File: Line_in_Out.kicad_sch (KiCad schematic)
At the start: 10 parts, among them J4 Out Left, J5 Out Right

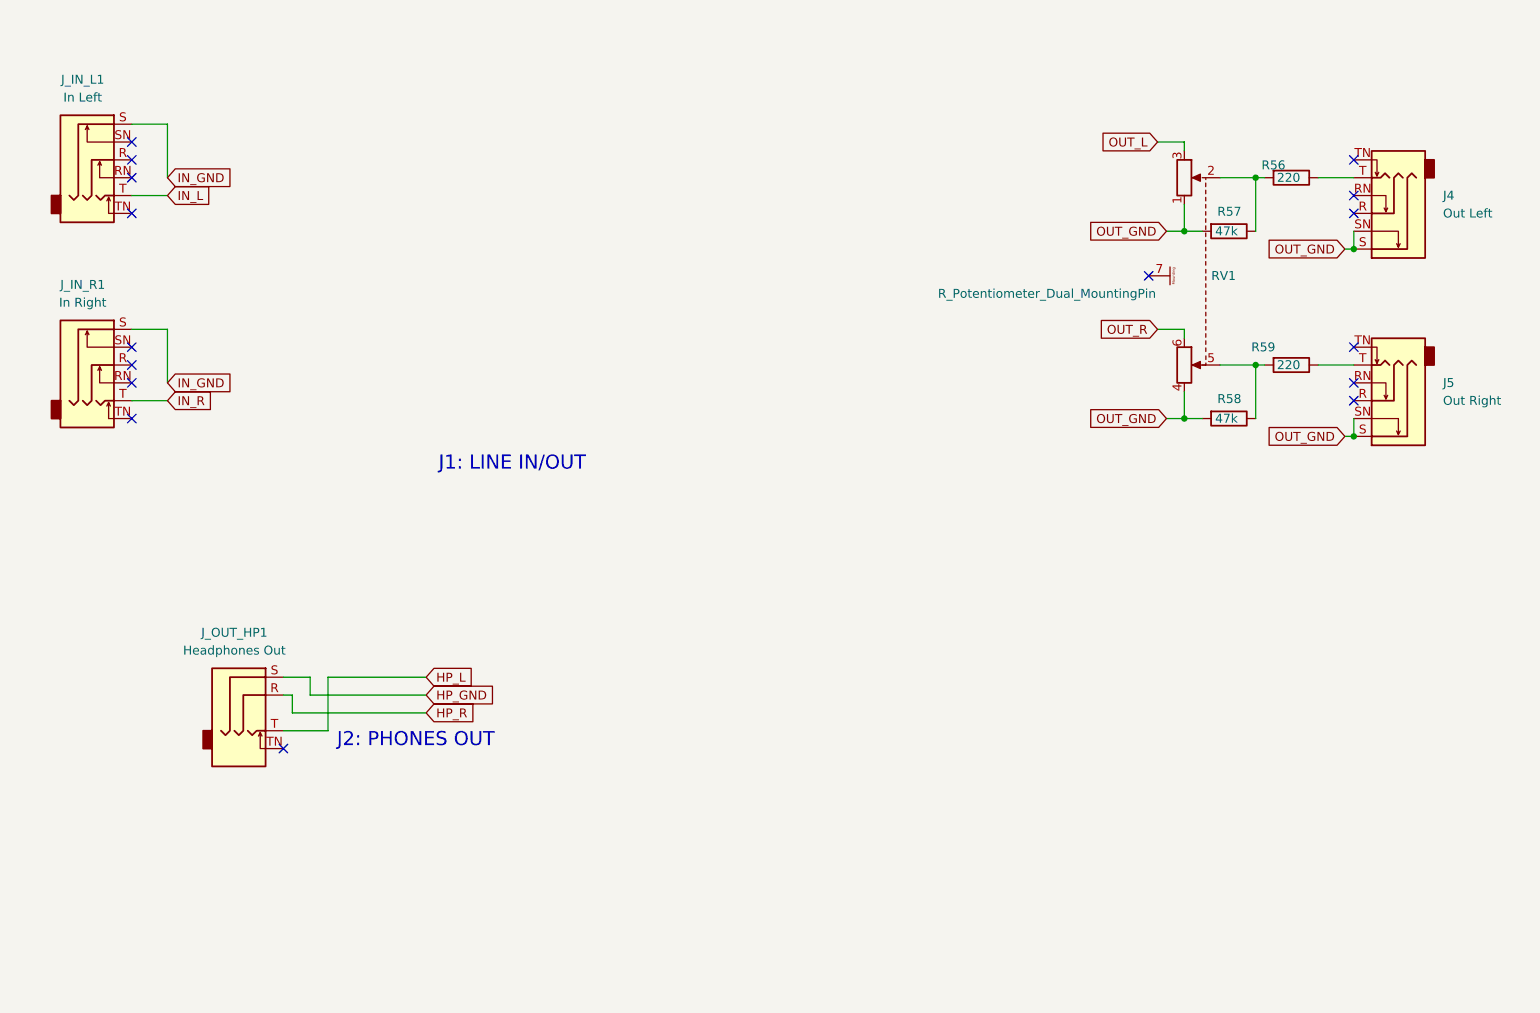
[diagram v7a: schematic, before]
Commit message: Added jack symbols and footprints also footprints for ics and caps
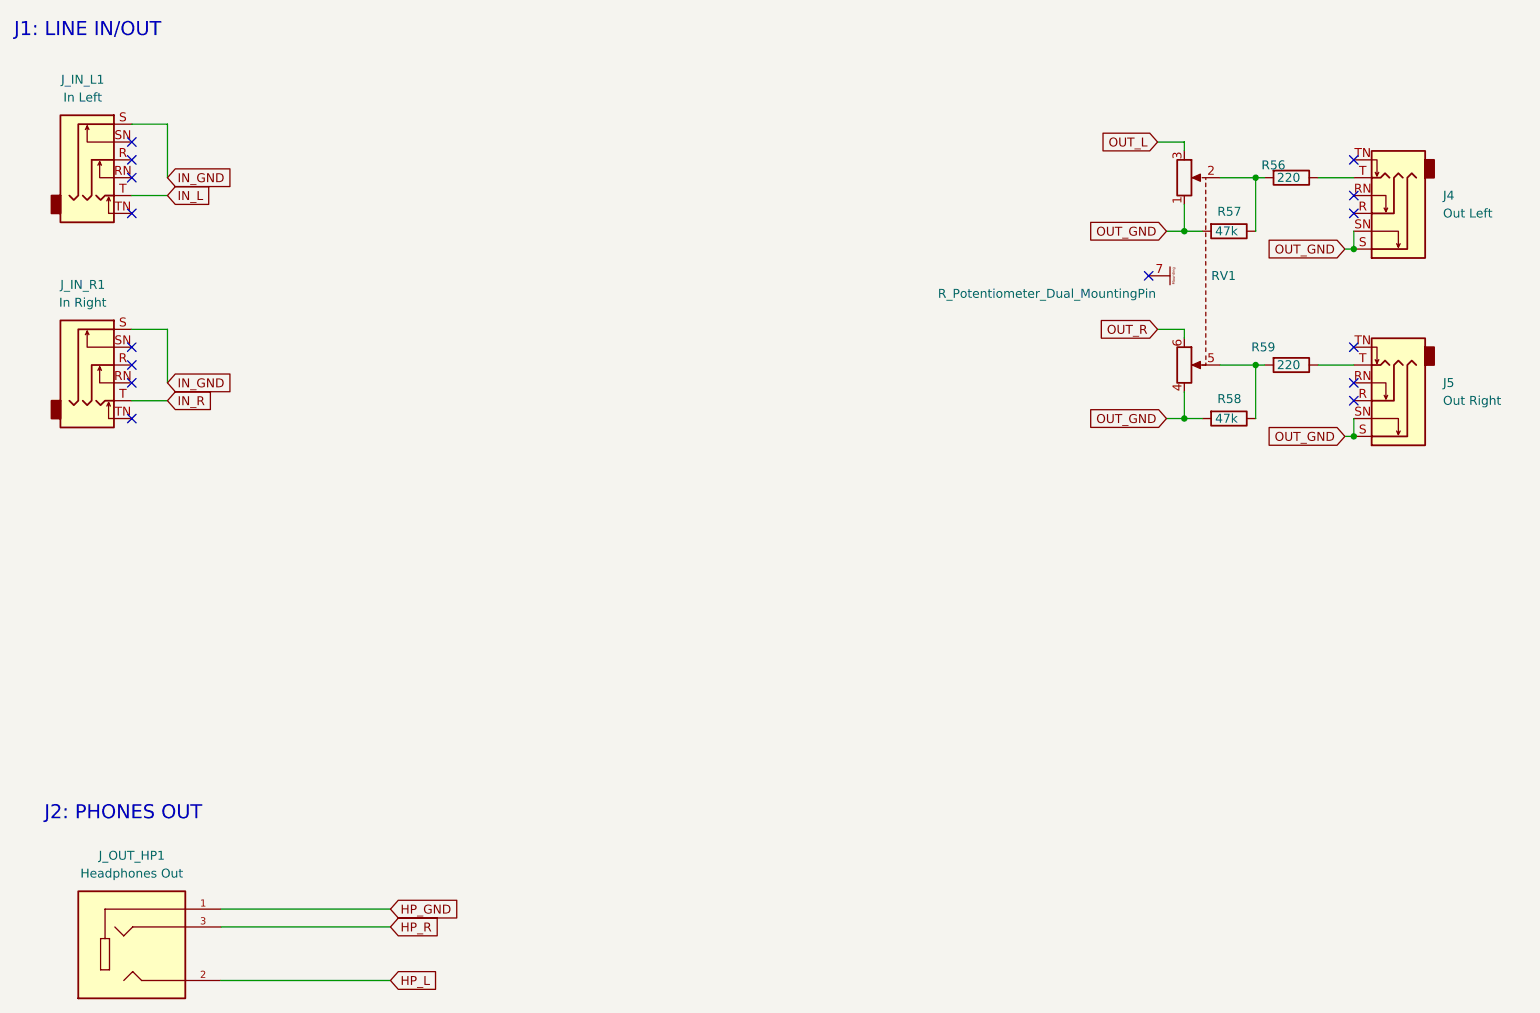
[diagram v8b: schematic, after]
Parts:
- J_OUT_HP1: footprint Connector_Audio:Jack_3.5mm_CUI_SJ1-3513N_Horizontal -> diggi_footprints:CUI_SJ1-3523N; symbol ksoloti_shield_symbols:AudioJack3_3.5mm_Stereo_SwitchT_WQP729JH-Blue_from_Thonk -> SJ1-3523N:SJ1-3523N; Availability (none) -> In Stock; Check_prices (none) -> https://www.snapeda.com/parts/SJ1-3523N/Same+Sky/view-part/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; Description_1 (none) -> 3.5 mm, Stereo, Right Angle, Through Hole, 3 Conductors, 0 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; MANUFACTURER (none) -> CUI Devices; MAXIMUM_PACKAGE_HEIGHT (none) -> 6.25 mm; MF (none) -> Same Sky; MP (none) -> SJ1-3523N; PARTREV (none) -> 1.05; Package (none) -> None; Price (none) -> None; Purchase-URL (none) -> https://www.snapeda.com/api/url_track_click_mouser/?unipart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; STANDARD (none) -> Manufacturer Recommendations; SnapEDA_Link (none) -> https://www.snapeda.com/parts/SJ1-3523N/Same+Sky/view-part/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
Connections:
- net HP_GND: now also J_OUT_HP1.1; no longer J_OUT_HP1.S
- net HP_L: now also J_OUT_HP1.2; no longer J_OUT_HP1.T
- net HP_R: now also J_OUT_HP1.3; no longer J_OUT_HP1.R
- no-connect marks 16 -> 15
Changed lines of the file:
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@@
 	(text "J2: PHONES OUT"
 		(exclude_from_sim no)
-		(at 87.63 128.27 0)
+		(at 45.974 138.684 0)
 		(effects
 			(font
@@
 	(text "J1: LINE IN/OUT"
 		(exclude_from_sim no)
-		(at 102.108 88.9 0)
+		(at 41.656 27.178 0)
 		(effects
 			(font
@@
 	)
 	(no_connect
-		(at 80.01 128.27)
-	)
-	(no_connect
 		(at 232.41 44.45)
 	)
@@
 	(wire
 		(pts
+			(xy 71.12 161.29) (xy 95.25 161.29)
+		)
+		(stroke
+			(width 0)
+			(type default)
+		)
+	)
+	(wire
+		(pts
 			(xy 208.28 68.58) (xy 208.28 69.85)
 		)
@@
 	(wire
 		(pts
-			(xy 86.36 118.11) (xy 100.33 118.11)
+			(xy 71.12 153.67) (xy 95.25 153.67)
 		)
 		(stroke
@@
 	(wire
 		(pts
-			(xy 83.82 118.11) (xy 83.82 120.65)
-		)
-		(stroke
-			(width 0)
-			(type default)
-		)
-	)
-	(wire
-		(pts
-			(xy 80.01 120.65) (xy 81.28 120.65)
+			(xy 71.12 151.13) (xy 95.25 151.13)
 		)
 		(stroke
@@
 	(wire
 		(pts
-			(xy 83.82 120.65) (xy 100.33 120.65)
-		)
-		(stroke
-			(width 0)
-			(type default)
-		)
-	)
-	(wire
-		(pts
-			(xy 80.01 125.73) (xy 86.36 125.73)
-		)
-		(stroke
-			(width 0)
-			(type default)
-		)
-	)
-	(wire
-		(pts
 			(xy 208.28 50.8) (xy 208.28 54.61)
 		)
@@
 	(wire
 		(pts
-			(xy 81.28 120.65) (xy 81.28 123.19)
-		)
-		(stroke
-			(width 0)
-			(type default)
-		)
-	)
-	(wire
-		(pts
-			(xy 81.28 123.19) (xy 100.33 123.19)
-		)
-		(stroke
-			(width 0)
-			(type default)
-		)
-	)
-	(wire
-		(pts
 			(xy 58.42 49.53) (xy 63.5 49.53)
 		)
@@
 		(pts
 			(xy 208.28 54.61) (xy 210.82 54.61)
-		)
-		(stroke
-			(width 0)
-			(type default)
-		)
-	)
-	(wire
-		(pts
-			(xy 80.01 118.11) (xy 83.82 118.11)
-		)
-		(stroke
-			(width 0)
-			(type default)
-		)
-	)
-	(wire
-		(pts
-			(xy 86.36 125.73) (xy 86.36 118.11)
 		)
 		(stroke
@@
 	(global_label "HP_R"
 		(shape input)
-		(at 100.33 123.19 0)
+		(at 95.25 153.67 0)
 		(fields_autoplaced yes)
 		(effects
@@
 		)
 		(property "Intersheetrefs" "${INTERSHEET_REFS}"
-			(at 107.5812 123.1106 0)
+			(at 102.5012 153.5906 0)
 			(effects
 				(font
@@
 	(global_label "HP_L"
 		(shape input)
-		(at 100.33 118.11 0)
+		(at 95.25 161.29 0)
 		(fields_autoplaced yes)
 		(effects
@@
 		)
 		(property "Intersheetrefs" "${INTERSHEET_REFS}"
-			(at 107.3393 118.0306 0)
+			(at 102.2593 161.2106 0)
 			(effects
 				(font
@@
 	(global_label "HP_GND"
 		(shape input)
-		(at 100.33 120.65 0)
+		(at 95.25 151.13 0)
 		(fields_autoplaced yes)
 		(effects
@@
 		)
 		(property "Intersheetrefs" "${INTERSHEET_REFS}"
-			(at 110.1817 120.5706 0)
+			(at 105.1017 151.0506 0)
 			(effects
 				(font
@@
 	)
 	(symbol
-		(lib_id "ksoloti_shield_symbols:AudioJack3_3.5mm_Stereo_SwitchT_WQP729JH-Blue_from_Thonk")
-		(at 74.93 120.65 0)
+		(lib_id "SJ1-3523N:SJ1-3523N")
+		(at 58.42 156.21 0)
 		(unit 1)
 		(exclude_from_sim no)
@@
 		(fields_autoplaced yes)
 		(property "Reference" "J_OUT_HP1"
-			(at 73.025 111.76 0)
+			(at 58.42 143.51 0)
 			(effects
 				(font
@@
 		)
 		(property "Value" "Headphones Out"
-			(at 73.025 114.3 0)
-			(effects
-				(font
-					(size 1.27 1.27)
-				)
-			)
-		)
-		(property "Footprint" "Connector_Audio:Jack_3.5mm_CUI_SJ1-3513N_Horizontal"
-			(at 74.93 120.65 0)
-			(effects
-				(font
-					(size 1.27 1.27)
-				)
+			(at 58.42 146.05 0)
+			(effects
+				(font
+					(size 1.27 1.27)
+				)
+			)
+		)
+		(property "Footprint" "diggi_footprints:CUI_SJ1-3523N"
+			(at 58.42 156.21 0)
+			(effects
+				(font
+					(size 1.27 1.27)
+				)
+				(justify bottom)
 				(hide yes)
 			)
 		)
 		(property "Datasheet" "~"
-			(at 74.93 120.65 0)
+			(at 58.42 156.21 0)
 			(effects
 				(font
@@
 		)
 		(property "Description" "Audio Jack, 3 Poles (Stereo / TRS), Switched TR Poles (Normalling)"
-			(at 74.93 120.65 0)
-			(effects
-				(font
-					(size 1.27 1.27)
-				)
-				(hide yes)
-			)
-		)
-		(pin "R"
-		)
-		(pin "T"
-		)
-		(pin "S"
-		)
-		(pin "TN"
+			(at 58.42 156.21 0)
+			(effects
+				(font
+					(size 1.27 1.27)
+				)
+				(hide yes)
+			)
+		)
+		(property "MF" "Same Sky"
+			(at 58.42 156.21 0)
+			(effects
+				(font
+					(size 1.27 1.27)
+				)
+				(justify bottom)
+				(hide yes)
+			)
+		)
+		(property "MAXIMUM_PACKAGE_HEIGHT" "6.25 mm"
+			(at 58.42 156.21 0)
+			(effects
+				(font
+					(size 1.27 1.27)
+				)
+				(justify bottom)
+				(hide yes)
+			)
+		)
+		(property "Package" "None"
+			(at 58.42 156.21 0)
+			(effects
+				(font
+					(size 1.27 1.27)
+				)
+				(justify bottom)
+				(hide yes)
+			)
+		)
+		(property "Price" "None"
+			(at 58.42 156.21 0)
+			(effects
+				(font
+					(size 1.27 1.27)
+				)
+				(justify bottom)
+				(hide yes)
+			)
+		)
+		(property "Check_prices" "https://www.snapeda.com/parts/SJ1-3523N/Same+Sky/view-part/?ref=eda"
+			(at 58.42 156.21 0)
+			(effects
+				(font
+					(size 1.27 1.27)
+				)
+				(justify bottom)
+				(hide yes)
+			)
+		)
+		(property "STANDARD" "Manufacturer Recommendations"
+			(at 58.42 156.21 0)
+			(effects
+				(font
+					(size 1.27 1.27)
+				)
+				(justify bottom)
+				(hide yes)
+			)
+		)
+		(property "PARTREV" "1.05"
+			(at 58.42 156.21 0)
+			(effects
+				(font
+					(size 1.27 1.27)
+				)
+				(justify bottom)
+				(hide yes)
+			)
+		)
+		(property "SnapEDA_Link" "https://www.snapeda.com/parts/SJ1-3523N/Same+Sky/view-part/?ref=snap"
+			(at 58.42 156.21 0)
+			(effects
+				(font
+					(size 1.27 1.27)
+				)
+				(justify bottom)
+				(hide yes)
+			)
+		)
+		(property "MP" "SJ1-3523N"
+			(at 58.42 156.21 0)
+			(effects
+				(font
+					(size 1.27 1.27)
+				)
+				(justify bottom)
+				(hide yes)
+			)
+		)
+		(property "Purchase-URL" "https://www.snapeda.com/api/url_track_click_mouser/?unipart_id=45488&manufacturer=Same Sky&part_name=SJ1-3523N&search_term=None"
+			(at 58.42 156.21 0)
+			(effects
+				(font
+					(size 1.27 1.27)
+				)
+				(justify bottom)
+				(hide yes)
+			)
+		)
+		(property "Description_1" "3.5 mm, Stereo, Right Angle, Through Hole, 3 Conductors, 0 Internal Switches, Audio Jack Connector"
+			(at 58.42 156.21 0)
+			(effects
+				(font
+					(size 1.27 1.27)
+				)
+				(justify bottom)
+				(hide yes)
+			)
+		)
+		(property "Availability" "In Stock"
+			(at 58.42 156.21 0)
+			(effects
+				(font
+					(size 1.27 1.27)
+				)
+				(justify bottom)
+				(hide yes)
+			)
+		)
+		(property "MANUFACTURER" "CUI Devices"
+			(at 58.42 156.21 0)
+			(effects
+				(font
+					(size 1.27 1.27)
+				)
+				(justify bottom)
+				(hide yes)
+			)
+		)
+		(pin "1"
+		)
+		(pin "3"
+		)
+		(pin "2"
 		)
 		(instances
